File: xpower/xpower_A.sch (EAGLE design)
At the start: 34 parts, among them U1 TLV70233, U2 TLV70225, U3 STM1061N29, U4 ADM1085, U5 LM3674-ADJ

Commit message: xpower: finished PCB.
Signed-off-by: malo <pavol.malosek@gmail.com>
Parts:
- added JP1: (no value), pinhead:PINHD-1X2
- added POR: TPTP14R, testpad:TPTP14R
- renumbered TP1 to PG_3V3
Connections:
- net +5V: now also JP1.2
- net GND: now also JP1.1
- net POR: now also POR.TP
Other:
- note added: "16.10.22.A"
- note added: "This work is licensed under a Creative Commons Attribution-ShareAlike 4.0 International License. http://creativecommons.org/licenses/by-sa/4.0/"
- note added: "http://25cmsquare.io"
- note removed: "LiWeBoard 16.10.22.A"
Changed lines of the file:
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@@
 <layer number="56" name="wert" color="7" fill="1" visible="no" active="no"/>
 <layer number="57" name="tCAD" color="7" fill="1" visible="no" active="no"/>
+<layer number="59" name="Invisible" color="7" fill="1" visible="no" active="no"/>
+<layer number="61" name="stand" color="7" fill="1" visible="no" active="no"/>
 <layer number="90" name="Modules" color="5" fill="1" visible="yes" active="yes"/>
 <layer number="91" name="Nets" color="2" fill="1" visible="yes" active="yes"/>
@@
 <layer number="127" name="_tValues" color="7" fill="1" visible="yes" active="yes"/>
 <layer number="128" name="_bValues" color="7" fill="1" visible="yes" active="yes"/>
+<layer number="130" name="bLogo" color="7" fill="1" visible="yes" active="yes"/>
 <layer number="131" name="tAdjust" color="7" fill="1" visible="yes" active="yes"/>
 <layer number="132" name="bAdjust" color="7" fill="1" visible="yes" active="yes"/>
@@
 <layer number="223" name="223bmp" color="24" fill="1" visible="no" active="no"/>
 <layer number="224" name="224bmp" color="25" fill="1" visible="no" active="no"/>
+<layer number="231" name="Eagle3D_PG1" color="14" fill="1" visible="yes" active="yes"/>
+<layer number="232" name="Eagle3D_PG2" color="14" fill="2" visible="yes" active="yes"/>
+<layer number="233" name="Eagle3D_PG3" color="14" fill="4" visible="yes" active="yes"/>
 <layer number="248" name="Housing" color="7" fill="1" visible="yes" active="yes"/>
 <layer number="249" name="Edge" color="7" fill="1" visible="yes" active="yes"/>
@@
 <part name="+3V7" library="supply1" deviceset="+3V3" device=""/>
 <part name="+2V3" library="25cmsquare" deviceset="+2V5" device=""/>
-<part name="TP1" library="testpad" deviceset="TP" device="TP14R"/>
+<part name="PG_3V3" library="testpad" deviceset="TP" device="TP14R"/>
 <part name="PE3" library="supply1" deviceset="PE" device=""/>
 <part name="GND26" library="supply1" deviceset="GND" device=""/>
@@
 <part name="+3V5" library="supply1" deviceset="+3V3" device=""/>
 <part name="U$4" library="25cmsquare" deviceset="+1V0" device=""/>
+<part name="POR" library="testpad" deviceset="TP" device="TP14R"/>
+<part name="JP1" library="pinhead" deviceset="PINHD-1X2" device=""/>
+<part name="P+7" library="supply1" deviceset="+5V" device=""/>
+<part name="GND22" library="supply1" deviceset="GND" device=""/>
 </parts>
 <sheets>
 <sheet>
 <plain>
-<text x="163.83" y="12.7" size="3.556" layer="94">LiWeBoard 16.10.22.A</text>
+<text x="173.99" y="12.7" size="3.556" layer="94">16.10.22.A</text>
+<text x="86.36" y="7.62" size="2.54" layer="94">This work is licensed under a Creative
+Commons Attribution-ShareAlike 4.0
+International License.
+http://creativecommons.org/licenses/by-sa/4.0/</text>
+<text x="215.9" y="20.32" size="2.54" layer="94">http://25cmsquare.io</text>
 </plain>
 <instances>
@@
 <attribute name="VALUE" x="60.96" y="134.62" size="1.778" layer="96"/>
 </instance>
-<instance part="TP1" gate="G$1" x="144.78" y="55.88" rot="R180"/>
+<instance part="PG_3V3" gate="G$1" x="144.78" y="55.88" rot="R180"/>
 <instance part="PE3" gate="M" x="88.9" y="104.14"/>
 <instance part="GND26" gate="1" x="109.22" y="104.14"/>
@@
 <attribute name="VALUE" x="20.32" y="17.78" size="1.778" layer="96" rot="MR90"/>
 </instance>
+<instance part="POR" gate="G$1" x="233.68" y="55.88" rot="R180"/>
+<instance part="JP1" gate="G$1" x="210.82" y="162.56" rot="R90"/>
+<instance part="P+7" gate="1" x="210.82" y="149.86" rot="R180"/>
+<instance part="GND22" gate="1" x="208.28" y="144.78" rot="MR0"/>
 </instances>
 <busses>
@@
 <pinref part="P+3" gate="1" pin="+5V"/>
 </segment>
+<segment>
+<pinref part="JP1" gate="G$1" pin="2"/>
+<wire x1="210.82" y1="160.02" x2="210.82" y2="152.4" width="0.1524" layer="91"/>
+<pinref part="P+7" gate="1" pin="+5V"/>
+</segment>
 </net>
 <net name="GND" class="0">
@@
 <pinref part="GND30" gate="1" pin="GND"/>
 </segment>
+<segment>
+<pinref part="JP1" gate="G$1" pin="1"/>
+<wire x1="208.28" y1="160.02" x2="208.28" y2="147.32" width="0.1524" layer="91"/>
+<pinref part="GND22" gate="1" pin="GND"/>
+</segment>
 </net>
 <net name="+3V3" class="0">
@@
 <label x="149.86" y="58.42" size="1.778" layer="95" xref="yes"/>
 <pinref part="R4" gate="G$1" pin="1"/>
-<pinref part="TP1" gate="G$1" pin="TP"/>
+<pinref part="PG_3V3" gate="G$1" pin="TP"/>
 </segment>
 <segment>
@@
 <segment>
 <pinref part="U4" gate="A" pin="EN_OUT"/>
-<wire x1="231.14" y1="58.42" x2="236.22" y2="58.42" width="0.1524" layer="91"/>
+<wire x1="231.14" y1="58.42" x2="233.68" y2="58.42" width="0.1524" layer="91"/>
 <label x="236.22" y="58.42" size="1.778" layer="95" xref="yes"/>
+<pinref part="POR" gate="G$1" pin="TP"/>
+<wire x1="233.68" y1="58.42" x2="236.22" y2="58.42" width="0.1524" layer="91"/>
+<junction x="233.68" y="58.42"/>
 </segment>
 <segment>
@@
 </schematic>
 </drawing>
+<compatibility>
+<note version="6.3" minversion="6.2.2" severity="warning">
+Since Version 6.2.2 text objects can contain more than one line,
+which will not be processed correctly with this version.
+</note>
+</compatibility>
 </eagle>

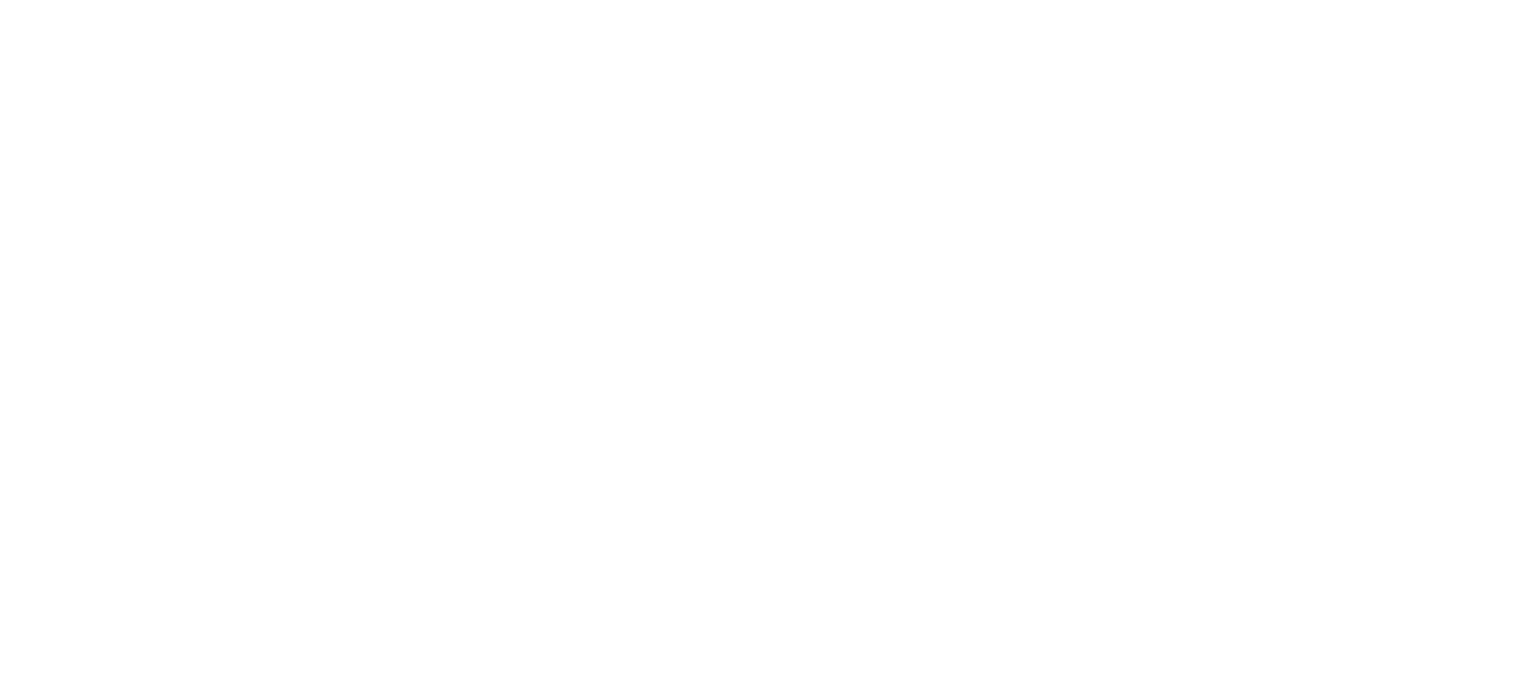
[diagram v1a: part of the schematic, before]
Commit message: xpower: BOM farnell lookup
Signed-off-by: malo <pavol.malosek@gmail.com>
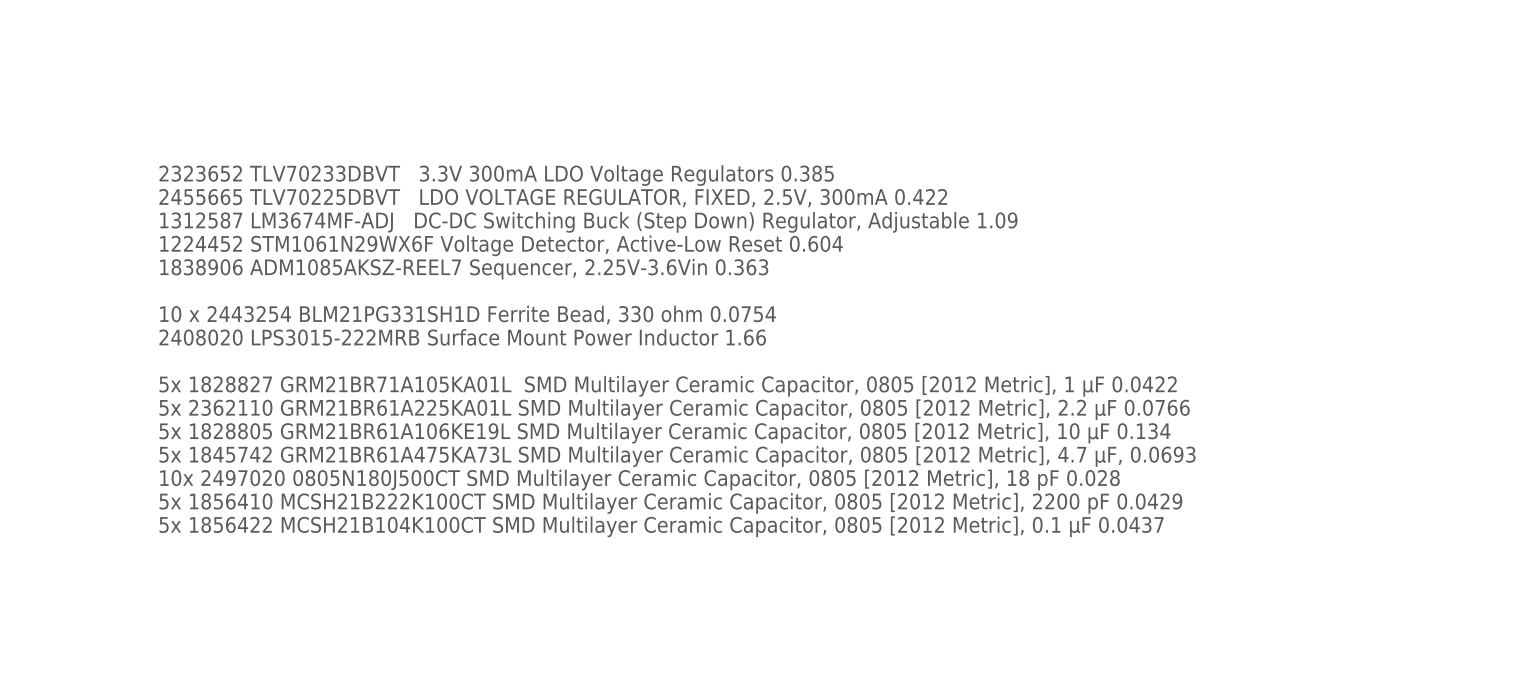
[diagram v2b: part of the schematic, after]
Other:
- note added: "2323652 TLV70233DBVT 3.3V 300mA LDO Voltage Regulators 0.385 2455665 TLV70225DBVT LDO VOLTAGE REGULATOR, FIXED, 2.5V, 300mA 0.422 1312587 LM3674MF-ADJ DC-DC Switching Buck (Step Down) Regulator, Adjustable 1.09 1224452 STM1061N29WX6F Voltage Detector, Active-Low Reset 0.604 1838906 ADM1085AKSZ-REEL7 Sequencer, 2.25V-3.6Vin 0.363 10 x 2443254 BLM21PG331SH1D Ferrite Bead, 330 ohm 0.0754 2408020 LPS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"
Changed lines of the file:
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@@
 http://creativecommons.org/licenses/by-sa/4.0/</text>
 <text x="215.9" y="20.32" size="2.54" layer="94">http://25cmsquare.io</text>
+<text x="266.7" y="93.98" size="1.778" layer="97">2323652 TLV70233DBVT   3.3V 300mA LDO Voltage Regulators 0.385
+2455665 TLV70225DBVT   LDO VOLTAGE REGULATOR, FIXED, 2.5V, 300mA 0.422
+1312587 LM3674MF-ADJ   DC-DC Switching Buck (Step Down) Regulator, Adjustable 1.09
+1224452 STM1061N29WX6F Voltage Detector, Active-Low Reset 0.604
+1838906 ADM1085AKSZ-REEL7 Sequencer, 2.25V-3.6Vin 0.363
+10 x 2443254 BLM21PG331SH1D Ferrite Bead, 330 ohm 0.0754
+2408020 LPS3015-222MRB Surface Mount Power Inductor 1.66
+5x 1828827 GRM21BR71A105KA01L  SMD Multilayer Ceramic Capacitor, 0805 [2012 Metric], 1 µF 0.0422
+5x 2362110 GRM21BR61A225KA01L SMD Multilayer Ceramic Capacitor, 0805 [2012 Metric], 2.2 µF 0.0766
+5x 1828805 GRM21BR61A106KE19L SMD Multilayer Ceramic Capacitor, 0805 [2012 Metric], 10 µF 0.134
+5x 1845742 GRM21BR61A475KA73L SMD Multilayer Ceramic Capacitor, 0805 [2012 Metric], 4.7 µF, 0.0693
+10x 2497020 0805N180J500CT SMD Multilayer Ceramic Capacitor, 0805 [2012 Metric], 18 pF 0.028
+5x 1856410 MCSH21B222K100CT SMD Multilayer Ceramic Capacitor, 0805 [2012 Metric], 2200 pF 0.0429
+5x 1856422 MCSH21B104K100CT SMD Multilayer Ceramic Capacitor, 0805 [2012 Metric], 0.1 µF 0.0437
+</text>
 </plain>
 <instances>

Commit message: xpower: minor beautifications
Signed-off-by: malo <pavol.malosek@gmail.com>
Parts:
- C11: value 0.1u, 0805 -> 100n, 0805
- PWR1: device 25cmsquare:LIWE_12_PIN_PWR -> 25cmsquare:LIWE_12_PIN_PWR5X5
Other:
- note added: "10x 1828827 GRM21BR71A105KA01L SMD Multilayer Ceramic Capacitor, 0805 1 µF, 10 V £0.0422 10x 1828923 GRM21BR71A225KA01L SMD Multilayer Ceramic Capacitor, 0805 2.2 µF, 10 V £0.0772 10x 1856422 MCSH21B104K100CT SMD Multilayer Ceramic Capacitor, 0805 0.1 µF, 10 V £0.0466 10x 1759420 MC0805X475K100CT SMD Multilayer Ceramic Capacitor, 0805 4.7 µF, 10 V £0.0547 10x 1828828 GRM21BR71A106KE51L SMD Multil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"
- note added: "2323652 TLV70233DBVT 3.3V 300mA LDO Voltage Regulators 0.385 2455665 TLV70225DBVT LDO VOLTAGE REGULATOR, FIXED, 2.5V, 300mA 0.422 1312587 LM3674MF-ADJ DC-DC Switching Buck (Step Down) Regulator, Adjustable 1.09 1224452 STM1061N29WX6F Voltage Detector, Active-Low Reset 0.604 1838906 ADM1085AKSZ-REEL7 Sequencer, 2.25V-3.6Vin 0.363 2408020 LPS3015-222MRB Surface Mount Power Inductor 1.66"
- note removed: "2323652 TLV70233DBVT 3.3V 300mA LDO Voltage Regulators 0.385 2455665 TLV70225DBVT LDO VOLTAGE REGULATOR, FIXED, 2.5V, 300mA 0.422 1312587 LM3674MF-ADJ DC-DC Switching Buck (Step Down) Regulator, Adjustable 1.09 1224452 STM1061N29WX6F Voltage Detector, Active-Low Reset 0.604 1838906 ADM1085AKSZ-REEL7 Sequencer, 2.25V-3.6Vin 0.363 10 x 2443254 BLM21PG331SH1D Ferrite Bead, 330 ohm 0.0754 2408020 LPS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"
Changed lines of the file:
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@@
 <part name="U1" library="25cmsquare" deviceset="TLV702" device="" value="TLV70233"/>
 <part name="FRAME1" library="frames" deviceset="A4L-LOC" device=""/>
-<part name="PWR1" library="25cmsquare" deviceset="LIWE_12_PIN_PWR" device=""/>
+<part name="PWR1" library="25cmsquare" deviceset="LIWE_12_PIN_PWR" device="5X5"/>
 <part name="P+1" library="supply1" deviceset="+5V" device=""/>
 <part name="GND1" library="supply1" deviceset="GND" device=""/>
@@
 <part name="C7" library="rcl" deviceset="C-EU" device="C0805" value="1u, 0805"/>
 <part name="C10" library="rcl" deviceset="C-EU" device="C0805" value="2u2, 0805"/>
-<part name="C11" library="rcl" deviceset="C-EU" device="C0805" value="0.1u, 0805"/>
+<part name="C11" library="rcl" deviceset="C-EU" device="C0805" value="100n, 0805"/>
 <part name="C12" library="rcl" deviceset="C-EU" device="C0805" value="2n2, 0805"/>
 <part name="C13" library="rcl" deviceset="C-EU" device="C0805" value="4.7u, 0805"/>
@@
 1224452 STM1061N29WX6F Voltage Detector, Active-Low Reset 0.604
 1838906 ADM1085AKSZ-REEL7 Sequencer, 2.25V-3.6Vin 0.363
-10 x 2443254 BLM21PG331SH1D Ferrite Bead, 330 ohm 0.0754
-2408020 LPS3015-222MRB Surface Mount Power Inductor 1.66
-5x 1828827 GRM21BR71A105KA01L  SMD Multilayer Ceramic Capacitor, 0805 [2012 Metric], 1 µF 0.0422
-5x 2362110 GRM21BR61A225KA01L SMD Multilayer Ceramic Capacitor, 0805 [2012 Metric], 2.2 µF 0.0766
-5x 1828805 GRM21BR61A106KE19L SMD Multilayer Ceramic Capacitor, 0805 [2012 Metric], 10 µF 0.134
-5x 1845742 GRM21BR61A475KA73L SMD Multilayer Ceramic Capacitor, 0805 [2012 Metric], 4.7 µF, 0.0693
-10x 2497020 0805N180J500CT SMD Multilayer Ceramic Capacitor, 0805 [2012 Metric], 18 pF 0.028
-5x 1856410 MCSH21B222K100CT SMD Multilayer Ceramic Capacitor, 0805 [2012 Metric], 2200 pF 0.0429
-5x 1856422 MCSH21B104K100CT SMD Multilayer Ceramic Capacitor, 0805 [2012 Metric], 0.1 µF 0.0437
-</text>
+2408020 LPS3015-222MRB Surface Mount Power Inductor 1.66</text>
+<text x="266.7" y="66.04" size="1.778" layer="97">10x 1828827 GRM21BR71A105KA01L SMD Multilayer Ceramic Capacitor, 0805 1 µF, 10 V    £0.0422
+10x 1828923 GRM21BR71A225KA01L SMD Multilayer Ceramic Capacitor, 0805 2.2 µF, 10 V  £0.0772
+10x 1856422 MCSH21B104K100CT   SMD Multilayer Ceramic Capacitor, 0805 0.1 µF, 10 V  £0.0466
+10x 1759420 MC0805X475K100CT   SMD Multilayer Ceramic Capacitor, 0805 4.7 µF, 10 V  £0.0547
+10x 1828828 GRM21BR71A106KE51L SMD Multilayer Ceramic Capacitor, 0805 10 µF, 10 V,  £0.193
+10x 1856410 MCSH21B222K100CT   SMD Multilayer Ceramic Capacitor, 0805 2200 pF, 10 V £0.0457
+10x 1759194 MC0805N180J500CT   SMD Multilayer Ceramic Capacitor, 0805 18 pF, 50V    £0.0156
+10x 2443254 BLM21PG331SH1D     Ferrite Bead, 330 ohm, 0805 1.5 A, 0.07 ohm          £0.0658
+5x  2554981 ZX62D-B-5PA8(30)   USB Connector, Micro USB Type B, USB 2.0,            £0.56</text>
 </plain>
 <instances>
